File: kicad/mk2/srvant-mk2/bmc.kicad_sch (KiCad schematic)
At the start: 38 parts, among them J3 Conn_01x03, J4 USB_OTG, J7 Conn_02x05_Odd_Even, SW1 POWER, SW2 EMMC_KEY, SW3 RST, SW4 HOST_RESET, U22 TMP1075DSG, U25 74AHC1G08, U5 rp-t113-s3, U6 PCF85063AT/AAZ, U7 TPD4EUSB30, U8 74LVC2G07, Y1 X32K768S301

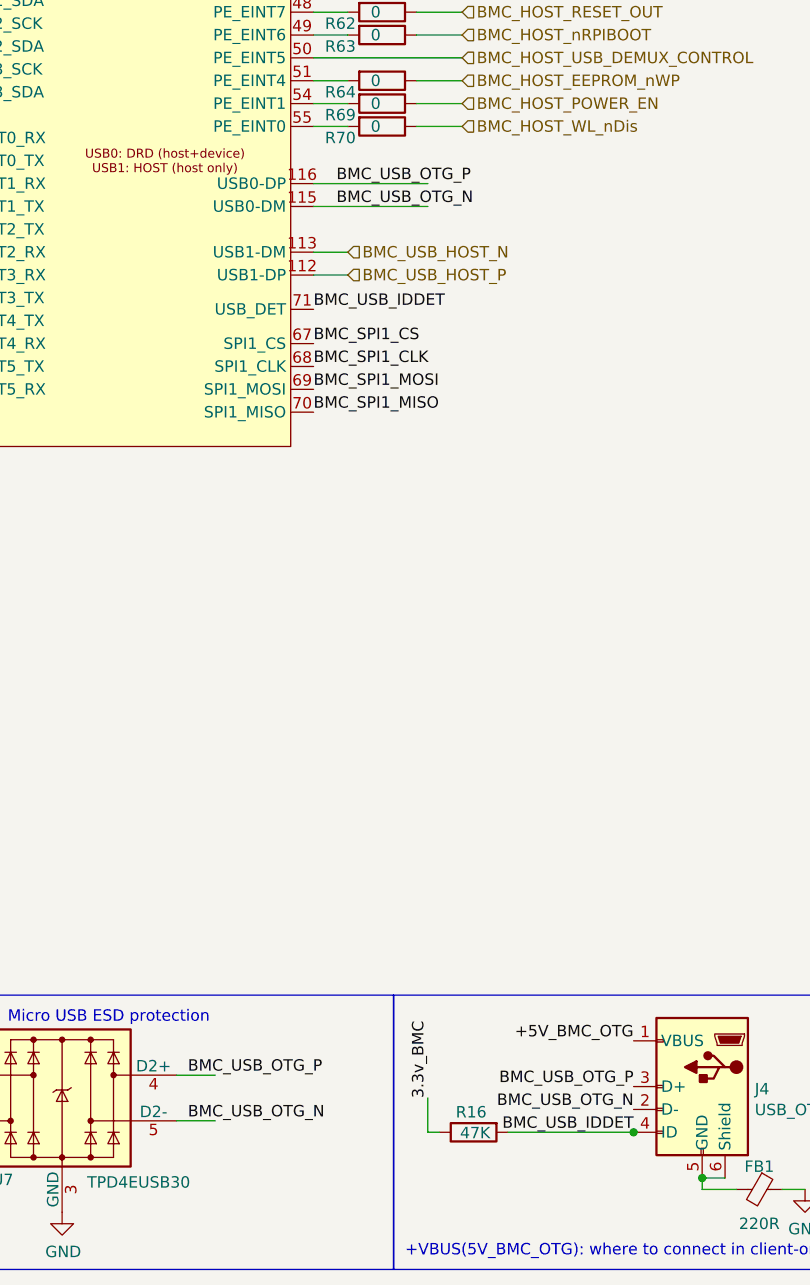
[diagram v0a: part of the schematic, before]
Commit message: reroute diff pairs
Reroute all diff pairs after another run with the jlcpcb calculator.
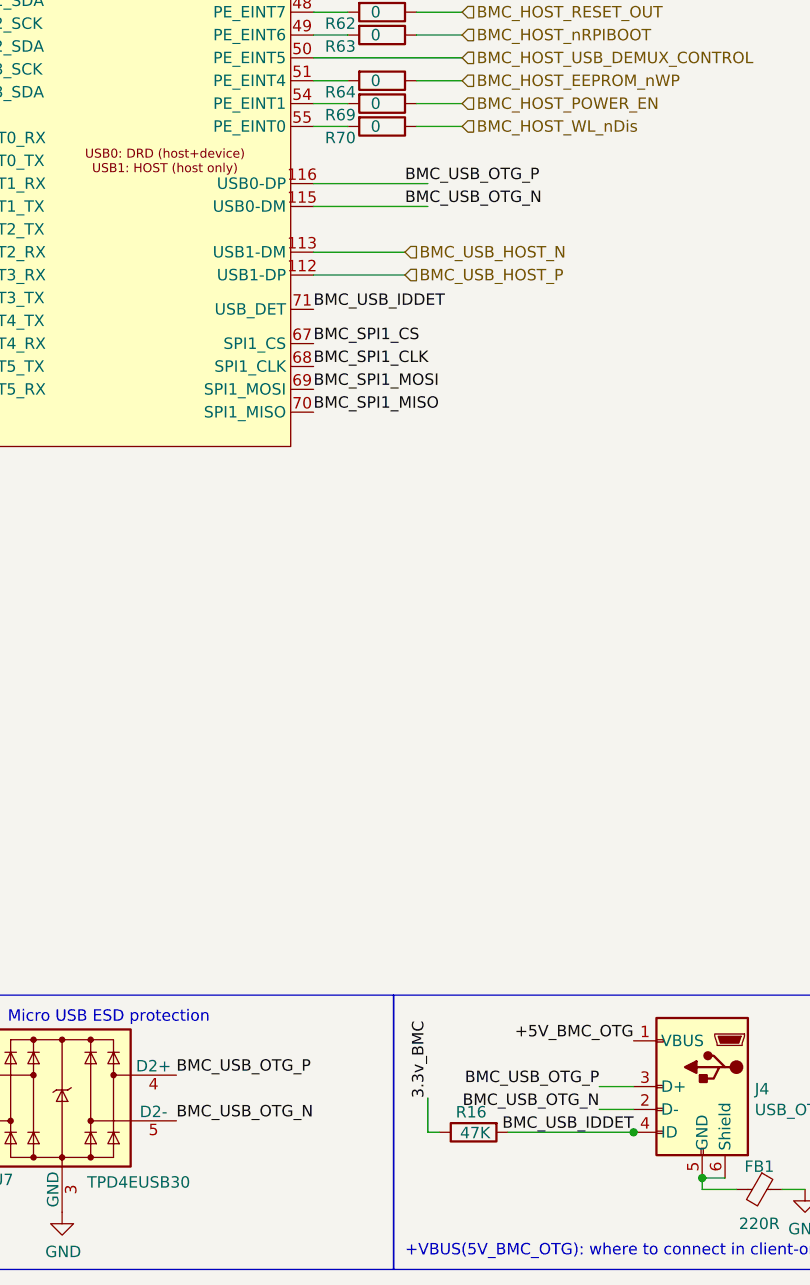
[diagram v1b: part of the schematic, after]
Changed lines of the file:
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@@
     (stroke (width 0) (type default))
   )
-  (wire (pts (xy 214.63 160.02) (xy 218.44 160.02))
+  (wire (pts (xy 214.63 160.02) (xy 224.79 160.02))
     (stroke (width 0) (type default))
   )
@@
     (stroke (width 0) (type default))
   )
-  (wire (pts (xy 214.63 152.4) (xy 227.33 152.4))
-    (stroke (width 0) (type default))
-  )
   (wire (pts (xy 48.26 157.48) (xy 48.26 160.02))
     (stroke (width 0) (type default))
@@
     (stroke (width 0) (type default))
   )
-  (wire (pts (xy 199.39 256.54) (xy 203.708 256.54))
-    (stroke (width 0) (type solid))
-  )
-  (wire (pts (xy 199.39 251.46) (xy 203.708 251.46))
-    (stroke (width 0) (type solid))
-  )
   (wire (pts (xy 45.72 96.52) (xy 48.26 96.52))
     (stroke (width 0) (type default))
@@
     (stroke (width 0) (type default))
   )
-  (wire (pts (xy 214.63 162.56) (xy 218.44 162.56))
+  (wire (pts (xy 214.63 162.56) (xy 224.79 162.56))
     (stroke (width 0) (type default))
   )
@@
     (stroke (width 0) (type default))
   )
+  (wire (pts (xy 246.38 255.27) (xy 250.19 255.27))
+    (stroke (width 0) (type default))
+  )
   (wire (pts (xy 378.46 43.18) (xy 378.46 40.64))
     (stroke (width 0) (type default))
@@
     (stroke (width 0) (type default))
   )
+  (wire (pts (xy 246.38 252.73) (xy 250.19 252.73))
+    (stroke (width 0) (type default))
+  )
   (wire (pts (xy 106.68 45.72) (xy 109.22 45.72))
     (stroke (width 0) (type default))
@@
     (stroke (width 0) (type solid))
   )
+  (wire (pts (xy 214.63 152.4) (xy 227.33 152.4))
+    (stroke (width 0) (type default))
+  )
   (wire (pts (xy 48.26 162.56) (xy 48.26 165.1))
     (stroke (width 0) (type default))
@@
     (effects (font (size 1.27 1.27)) (justify left bottom))
   )
-  (label "BMC_USB_OTG_P" (at 217.17 152.4 0) (fields_autoplaced)
+  (label "BMC_USB_OTG_P" (at 224.79 152.4 0)
     (effects (font (size 1.27 1.27)) (justify left bottom))
+    (property "Netclass" "90R" (at 218.44 151.13 0)
+      (effects (font (size 1.27 1.27) italic) (justify left))
+    )
   )
   (label "3.3v_BMC" (at 339.09 25.4 0) (fields_autoplaced)
@@
     (effects (font (size 1.27 1.27)) (justify right bottom))
   )
-  (label "BMC_USB_OTG_P" (at 250.19 252.73 180) (fields_autoplaced)
+  (label "BMC_USB_OTG_P" (at 246.38 252.73 180)
     (effects (font (size 1.27 1.27)) (justify right bottom))
+    (property "Netclass" "90R" (at 250.19 251.46 0)
+      (effects (font (size 1.27 1.27) italic) (justify right))
+    )
   )
   (label "BMC_I2C_2_SCK" (at 172.72 134.62 180) (fields_autoplaced)
@@
     (effects (font (size 1.27 1.27)) (justify right bottom))
   )
-  (label "BMC_USB_OTG_P" (at 200.66 251.46 0) (fields_autoplaced)
+  (label "BMC_USB_OTG_P" (at 199.39 251.46 0) (fields_autoplaced)
     (effects (font (size 1.27 1.27)) (justify left bottom))
   )
@@
     (effects (font (size 1.27 1.27)) (justify right bottom))
   )
-  (label "BMC_USB_OTG_N" (at 200.66 256.54 0) (fields_autoplaced)
+  (label "BMC_USB_OTG_N" (at 199.39 256.54 0) (fields_autoplaced)
     (effects (font (size 1.27 1.27)) (justify left bottom))
   )
@@
     (effects (font (size 1.27 1.27)) (justify right bottom))
   )
-  (label "BMC_USB_OTG_N" (at 250.19 255.27 180) (fields_autoplaced)
+  (label "BMC_USB_OTG_N" (at 246.38 255.27 180)
     (effects (font (size 1.27 1.27)) (justify right bottom))
+    (property "Netclass" "90R" (at 250.19 254 0)
+      (effects (font (size 1.27 1.27) italic) (justify right))
+    )
   )
   (label "+5V_BMC_OTG" (at 250.19 247.65 180) (fields_autoplaced)
@@
     (effects (font (size 1.27 1.27)) (justify right bottom))
   )
-  (label "BMC_USB_OTG_N" (at 217.17 154.94 0) (fields_autoplaced)
+  (label "BMC_USB_OTG_N" (at 224.79 154.94 0)
     (effects (font (size 1.27 1.27)) (justify left bottom))
+    (property "Netclass" "90R" (at 218.44 153.67 0)
+      (effects (font (size 1.27 1.27) italic) (justify left))
+    )
   )
   (hierarchical_label "BMC_HOST_POWER_EN" (shape input) (at 231.14 143.51 0) (fields_autoplaced)
@@
     (effects (font (size 1.27 1.27)) (justify right))
   )
-  (hierarchical_label "BMC_USB_HOST_N" (shape input) (at 218.44 160.02 0) (fields_autoplaced)
+  (hierarchical_label "BMC_USB_HOST_N" (shape input) (at 224.79 160.02 0)
     (effects (font (size 1.27 1.27)) (justify left))
+    (property "Netclass" "90R" (at 220.98 158.75 0)
+      (effects (font (size 1.27 1.27) italic) (justify left))
+    )
   )
-  (hierarchical_label "BMC_USB_HOST_P" (shape input) (at 218.44 162.56 0) (fields_autoplaced)
+  (hierarchical_label "BMC_USB_HOST_P" (shape input) (at 224.79 162.56 0)
     (effects (font (size 1.27 1.27)) (justify left))
+    (property "Netclass" "90R" (at 220.98 161.29 0)
+      (effects (font (size 1.27 1.27) italic) (justify left))
+    )
   )
   (hierarchical_label "BMC_I2C_1_SDA" (shape output) (at 172.72 132.08 180) (fields_autoplaced)

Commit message: lot's of small updates
* fix the quartz footprint
* fix wrong inductor in pcie power unit
* fix lots of descriptions,uids
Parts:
- D9: farnell# (none) -> 4253959
- FB1: farnell# (none) -> 4236024
- U25: farnell# (none) -> 3120306
- Y1: footprint Crystal:Crystal_SMD_3215-2Pin_3.2x1.5mm -> PCM_Crystal_AKL:Crystal_SMD_2012-2Pin_2.0x1.2mm; Field7 AEL -> (none); digikey# (none) -> 535-14101-2-ND; manf# (none) -> ABS06W-32.768KHZ-K-2-T
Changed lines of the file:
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@@
       (effects (font (size 1.27 1.27)) hide)
     )
-    (property "farnell#" "" (at 264.16 264.16 0)
+    (property "farnell#" "4236024" (at 264.16 264.16 0)
       (effects (font (size 1.27 1.27)) hide)
     )
@@
       (effects (font (size 1.27 1.27)) (justify right))
     )
-    (property "Footprint" "Crystal:Crystal_SMD_3215-2Pin_3.2x1.5mm" (at 30.48 257.302 0)
-      (effects (font (size 1.27 1.27)) hide)
-    )
-    (property "Datasheet" "" (at 30.48 257.302 0)
+    (property "Footprint" "PCM_Crystal_AKL:Crystal_SMD_2012-2Pin_2.0x1.2mm" (at 30.48 257.302 0)
+      (effects (font (size 1.27 1.27)) hide)
+    )
+    (property "Datasheet" "https://abracon.com/Resonators/ABS06W.pdf" (at 30.48 257.302 0)
+      (effects (font (size 1.27 1.27)) hide)
+    )
+    (property "manf#" "ABS06W-32.768KHZ-K-2-T" (at 30.48 257.302 0)
+      (effects (font (size 1.27 1.27)) hide)
+    )
+    (property "digikey" "" (at 30.48 257.302 0)
+      (effects (font (size 1.27 1.27)) hide)
+    )
+    (property "Part Description" "Crystal 32.768KHz 7pF 20pmm" (at 30.48 257.302 0)
       (effects (font (size 1.27 1.27)) hide)
     )
@@
       (effects (font (size 1.27 1.27)) hide)
     )
-    (property "Field7" "AEL" (at 30.48 257.302 0)
-      (effects (font (size 1.27 1.27)) hide)
-    )
-    (property "Part Description" "Crystal 32.768KHz 7pF 20pmm" (at 30.48 257.302 0)
+    (property "digikey#" "535-14101-2-ND" (at 30.48 257.302 0)
       (effects (font (size 1.27 1.27)) hide)
     )
@@
       (effects (font (size 1.27 1.27)) hide)
     )
-    (property "farnell#" "" (at 133.35 43.18 0)
+    (property "farnell#" "3120306" (at 133.35 43.18 0)
       (effects (font (size 1.27 1.27)) hide)
     )
@@
       (effects (font (size 1.27 1.27)) hide)
     )
-    (property "farnell#" "" (at 67.31 50.8 0)
-      (effects (font (size 1.27 1.27)) hide)
-    )
+    (property "farnell#" "4253959" (at 67.31 50.8 0)
+      (effects (font (size 1.27 1.27)) hide)
+    )

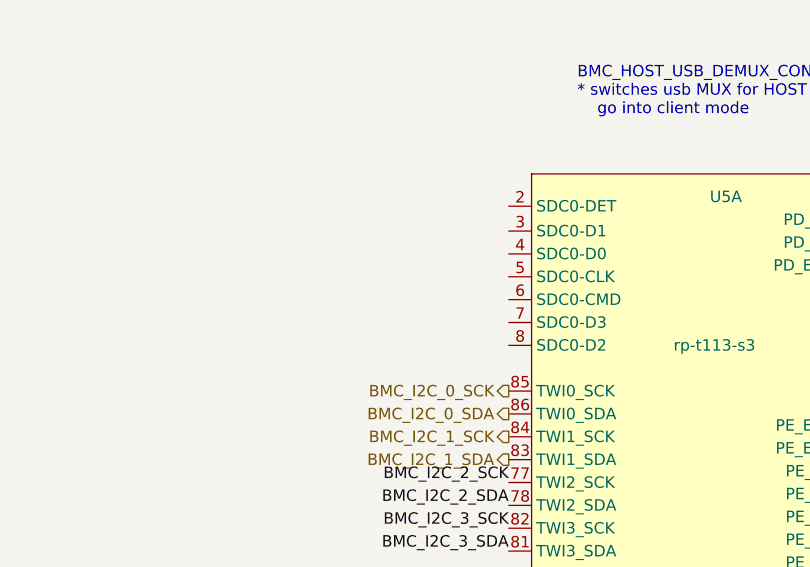
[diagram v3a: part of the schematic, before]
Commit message: add jtag pads, improve power lines
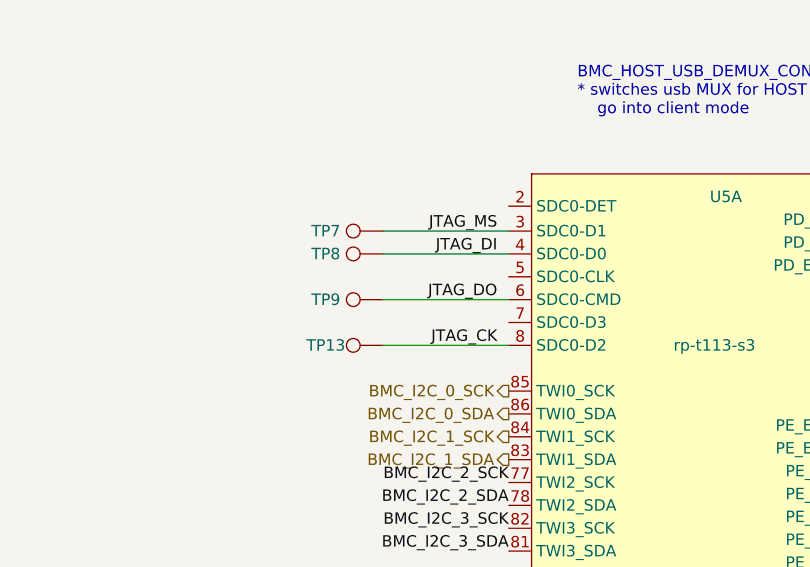
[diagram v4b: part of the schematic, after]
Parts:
- added TP13: CK, TestPoint:TestPoint_Pad_D1.0mm, symbol ARJM11:TestPoint
- added TP7: MS, TestPoint:TestPoint_Pad_D1.0mm, symbol ARJM11:TestPoint
- added TP8: DI, TestPoint:TestPoint_Pad_D1.0mm, symbol ARJM11:TestPoint
- added TP9: DO, TestPoint:TestPoint_Pad_D1.0mm, symbol ARJM11:TestPoint
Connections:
- net JTAG_MS: now reaches U5.3 (SDC0-D1)
- net JTAG_MS: now also TP7.1
- net JTAG_DI: now reaches U5.4 (SDC0-D0)
- net JTAG_DI: now also TP8.1
- net JTAG_DO: now reaches U5.6 (SDC0-CMD)
- net JTAG_DO: now also TP9.1
- net JTAG_CK: now reaches U5.8 (SDC0-D2)
- net JTAG_CK: now also TP13.1
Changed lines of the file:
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@@
     (stroke (width 0) (type default))
   )
+  (wire (pts (xy 158.75 114.3) (xy 172.72 114.3))
+    (stroke (width 0) (type default))
+  )
   (wire (pts (xy 48.26 170.18) (xy 48.26 172.72))
     (stroke (width 0) (type default))
@@
     (stroke (width 0) (type default))
   )
+  (wire (pts (xy 158.75 119.38) (xy 172.72 119.38))
+    (stroke (width 0) (type default))
+  )
   (wire (pts (xy 214.63 130.81) (xy 236.22 130.81))
     (stroke (width 0) (type default))
@@
     (stroke (width 0) (type default))
   )
+  (wire (pts (xy 158.75 106.68) (xy 172.72 106.68))
+    (stroke (width 0) (type default))
+  )
   (wire (pts (xy 227.33 254) (xy 227.33 257.81))
     (stroke (width 0) (type solid))
@@
     (stroke (width 0) (type default))
   )
+  (wire (pts (xy 158.75 109.22) (xy 172.72 109.22))
+    (stroke (width 0) (type default))
+  )
   (wire (pts (xy 106.68 45.72) (xy 109.22 45.72))
     (stroke (width 0) (type default))
@@
     )
   )
+  (label "JTAG_DO" (at 171.45 114.3 180) (fields_autoplaced)
+    (effects (font (size 1.27 1.27)) (justify right bottom))
+  )
   (label "BMC_I2C_2_SCK" (at 172.72 134.62 180) (fields_autoplaced)
     (effects (font (size 1.27 1.27)) (justify right bottom))
@@
     (effects (font (size 1.27 1.27)) (justify left bottom))
   )
+  (label "JTAG_DI" (at 171.45 109.22 180) (fields_autoplaced)
+    (effects (font (size 1.27 1.27)) (justify right bottom))
+  )
   (label "BMC_DEBUG_RX" (at 361.95 210.82 180) (fields_autoplaced)
     (effects (font (size 1.27 1.27)) (justify right bottom))
@@
     (effects (font (size 1.27 1.27)) (justify right bottom))
   )
+  (label "JTAG_CK" (at 171.45 119.38 180) (fields_autoplaced)
+    (effects (font (size 1.27 1.27)) (justify right bottom))
+  )
   (label "NMI_N" (at 64.77 262.89 0) (fields_autoplaced)
     (effects (font (size 1.27 1.27)) (justify left bottom))
@@
     (effects (font (size 1.27 1.27)) (justify right bottom))
   )
+  (label "JTAG_MS" (at 171.45 106.68 180) (fields_autoplaced)
+    (effects (font (size 1.27 1.27)) (justify right bottom))
+  )
   (label "3.3v_BMC" (at 229.87 50.8 0) (fields_autoplaced)
     (effects (font (size 1.27 1.27)) (justify left bottom))
@@
     )
   )
+  (symbol (lib_id "ARJM11:TestPoint") (at 158.75 109.22 90) (unit 1)
+    (in_bom yes) (on_board yes) (dnp no)
+    (property "Reference" "TP8" (at 152.4 109.22 90)
+      (effects (font (size 1.27 1.27)))
+    )
+    (property "Value" "DI" (at 155.448 106.68 90)
+      (effects (font (size 1.27 1.27)) hide)
+    )
+    (property "Footprint" "TestPoint:TestPoint_Pad_D1.0mm" (at 158.75 104.14 0)
+      (effects (font (size 1.27 1.27)) hide)
+    )
+    (property "Datasheet" "~" (at 158.75 104.14 0)
+      (effects (font (size 1.27 1.27)) hide)
+    )
+    (property "manf#" "" (at 158.75 109.22 0)
+      (effects (font (size 1.27 1.27)) hide)
+    )
+    (property "digikey#" "" (at 158.75 109.22 0)
+      (effects (font (size 1.27 1.27)) hide)
+    )
+    (property "mouser#" "" (at 158.75 109.22 0)
+      (effects (font (size 1.27 1.27)) hide)
+    )
+    (property "farnell#" "" (at 158.75 109.22 0)
+      (effects (font (size 1.27 1.27)) hide)
+    )
+    (property "rs#" "" (at 158.75 109.22 0)
+      (effects (font (size 1.27 1.27)) hide)
+    )
+    (property "Part Description" "" (at 158.75 109.22 0)
+      (effects (font (size 1.27 1.27)) hide)
+    )
+    (pin "1")
+    (instances
+      (project "srvant-mk2"
+        (path "/1859a578-b791-4142-bdf4-fda494df1146/a3ddce6d-c94c-48a5-9fee-a70fbee730bf"
+          (reference "TP8") (unit 1)
+        )
+      )
+    )
+  )
   (symbol (lib_id "74xGxx:74LVC2G07") (at 259.08 41.91 90) (unit 3)
     (in_bom yes) (on_board yes) (dnp no) (fields_autoplaced)
@@
     )
   )
+  (symbol (lib_id "ARJM11:TestPoint") (at 158.75 119.38 90) (unit 1)
+    (in_bom yes) (on_board yes) (dnp no)
+    (property "Reference" "TP13" (at 152.4 119.38 90)
+      (effects (font (size 1.27 1.27)))
+    )
+    (property "Value" "CK" (at 155.448 116.84 90)
+      (effects (font (size 1.27 1.27)) hide)
+    )
+    (property "Footprint" "TestPoint:TestPoint_Pad_D1.0mm" (at 158.75 114.3 0)
+      (effects (font (size 1.27 1.27)) hide)
+    )
+    (property "Datasheet" "~" (at 158.75 114.3 0)
+      (effects (font (size 1.27 1.27)) hide)
+    )
+    (property "manf#" "" (at 158.75 119.38 0)
+      (effects (font (size 1.27 1.27)) hide)
+    )
+    (property "digikey#" "" (at 158.75 119.38 0)
+      (effects (font (size 1.27 1.27)) hide)
+    )
+    (property "mouser#" "" (at 158.75 119.38 0)
+      (effects (font (size 1.27 1.27)) hide)
+    )
+    (property "farnell#" "" (at 158.75 119.38 0)
+      (effects (font (size 1.27 1.27)) hide)
+    )
+    (property "rs#" "" (at 158.75 119.38 0)
+      (effects (font (size 1.27 1.27)) hide)
+    )
+    (property "Part Description" "" (at 158.75 119.38 0)
+      (effects (font (size 1.27 1.27)) hide)
+    )
+    (pin "1")
+    (instances
+      (project "srvant-mk2"
+        (path "/1859a578-b791-4142-bdf4-fda494df1146/a3ddce6d-c94c-48a5-9fee-a70fbee730bf"
+          (reference "TP13") (unit 1)
+        )
+      )
+    )
+  )
   (symbol (lib_id "Device:R") (at 213.36 50.8 270) (unit 1)
     (in_bom yes) (on_board yes) (dnp no)
@@
     )
   )
+  (symbol (lib_id "ARJM11:TestPoint") (at 158.75 106.68 90) (unit 1)
+    (in_bom yes) (on_board yes) (dnp no)
+    (property "Reference" "TP7" (at 152.4 106.68 90)
+      (effects (font (size 1.27 1.27)))
+    )
+    (property "Value" "MS" (at 155.448 104.14 90)
+      (effects (font (size 1.27 1.27)) hide)
+    )
+    (property "Footprint" "TestPoint:TestPoint_Pad_D1.0mm" (at 158.75 101.6 0)
+      (effects (font (size 1.27 1.27)) hide)
+    )
+    (property "Datasheet" "~" (at 158.75 101.6 0)
+      (effects (font (size 1.27 1.27)) hide)
+    )
+    (property "manf#" "" (at 158.75 106.68 0)
+      (effects (font (size 1.27 1.27)) hide)
+    )
+    (property "digikey#" "" (at 158.75 106.68 0)
+      (effects (font (size 1.27 1.27)) hide)
+    )
+    (property "mouser#" "" (at 158.75 106.68 0)
+      (effects (font (size 1.27 1.27)) hide)
+    )
+    (property "farnell#" "" (at 158.75 106.68 0)
+      (effects (font (size 1.27 1.27)) hide)
+    )
+    (property "rs#" "" (at 158.75 106.68 0)
+      (effects (font (size 1.27 1.27)) hide)
+    )
+    (property "Part Description" "" (at 158.75 106.68 0)
+      (effects (font (size 1.27 1.27)) hide)
+    )
+    (pin "1")
+    (instances
+      (project "srvant-mk2"
+        (path "/1859a578-b791-4142-bdf4-fda494df1146/a3ddce6d-c94c-48a5-9fee-a70fbee730bf"
+          (reference "TP7") (unit 1)
+        )
+      )
+    )
+  )
   (symbol (lib_id "Device:R") (at 86.36 252.73 270) (mirror x) (unit 1)
     (in_bom yes) (on_board yes) (dnp no)
@@
         )
       )
+    )
+  )
+  (symbol (lib_id "ARJM11:TestPoint") (at 158.75 114.3 90) (unit 1)
+    (in_bom yes) (on_board yes) (dnp no)
+    (property "Reference" "TP9" (at 152.4 114.3 90)
+      (effects (font (size 1.27 1.27)))
+    )
+    (property "Value" "DO" (at 155.448 111.76 90)
+      (effects (font (size 1.27 1.27)) hide)
+    )
+    (property "Footprint" "TestPoint:TestPoint_Pad_D1.0mm" (at 158.75 109.22 0)
+      (effects (font (size 1.27 1.27)) hide)
+    )
+    (property "Datasheet" "~" (at 158.75 109.22 0)
+      (effects (font (size 1.27 1.27)) hide)
+    )
+    (property "manf#" "" (at 158.75 114.3 0)
+      (effects (font (size 1.27 1.27)) hide)
+    )
+    (property "digikey#" "" (at 158.75 114.3 0)
+      (effects (font (size 1.27 1.27)) hide)
+    )
+    (property "mouser#" "" (at 158.75 114.3 0)
+      (effects (font (size 1.27 1.27)) hide)
+    )
+    (property "farnell#" "" (at 158.75 114.3 0)
+      (effects (font (size 1.27 1.27)) hide)
+    )
+    (property "rs#" "" (at 158.75 114.3 0)
+      (effects (font (size 1.27 1.27)) hide)
+    )
+    (property "Part Description" "" (at 158.75 114.3 0)
+      (effects (font (size 1.27 1.27)) hide)
+    )
+    (pin "1")
+    (instances
+      (project "srvant-mk2"
+        (path "/1859a578-b791-4142-bdf4-fda494df1146/a3ddce6d-c94c-48a5-9fee-a70fbee730bf"
+          (reference "TP9") (unit 1)
+        )
+      )
